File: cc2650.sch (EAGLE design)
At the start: 22 parts, among them IC4 CC2650MODAMOHR, J1 AMP FCI 10103594-0001LF, SW1 SPST_TACT-KMR2, SW2 SPST_TACT-KMR2, U402 TPS62233DRY

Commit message: changed some pins. added bom through eagle.
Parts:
- removed BT1: (no value), SparkFun-Batteries:BATTERY-12MM_SMD
- removed D1: (no value), adafruit:SCHOTTKY-DIODEDO35-7
- removed J1: AMP FCI 10103594-0001LF, SparkFun-Connectors:USB_MICRO-B_HALF_PTH
- removed U$1: (no value), adafruit:CR1220THM
- added BAT: (no value), adafruit:CR1220THM
- added J401: (no value), usb_con-update:USB_MICRO_FLIPPED
- added R4: 100k, adafruit:R-US_R0603
- C1: MPN (none) -> C1005X7R1H104K050BB; OC_NEWARK (none) -> 04X3230
- C2: MPN (none) -> GRT31CC81E475KE01L; OC_NEWARK (none) -> 01AC8998
- C3, C4: MPN (none) -> C0805C105K5RACTU; OC_NEWARK (none) -> 05AC8016
- C5: MPN (none) -> CGA2B2C0G1H102J050BA; OC_NEWARK (none) -> 04X3142
- D2: MPN (none) -> CLMVB-FKA-CFHEHLCBB7A363; OC_NEWARK (none) -> 11X6434
- IC4: MPN (none) -> CC2650MODAMOHR; OC_NEWARK (none) -> 02AC9626
- JP2, JP3, SW1, SW2: OC_NEWARK (none) -> unknown
- JTAG_CONNECTOR: MPN (none) -> FTSH-105-01-F-DV-K; OC_NEWARK (none) -> 45P5160
- L401: MPN (none) -> NR3010T2R2M; OC_NEWARK (none) -> 87K4752
- LED3: MPN (none) -> HSME-C191; OC_NEWARK (none) -> 05M0345
- R1: MF (none) -> VISHAY/DALE; MPN (none) -> CRCW040247K0JNED; OC_NEWARK (none) -> 52K7099
- R2: MPN (none) -> ERA-2AEB471X; OC_NEWARK (none) -> 08N2086
- R3: MPN (none) -> ERJ-U02F33R0X; OC_NEWARK (none) -> 51W3197
- U402: MPN (none) -> TPS62233DRYT; OC_NEWARK (none) -> 37X8886
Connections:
- removed net EZFET_VBUS: C1.1, C2.1, C3.1, D1.C, J1.VBUS, U402.EN, U402.VIN
- removed net N$10: J1.SHIELD, R3.1
- removed net N$3: BT1.+, D1.A
- new net EN: JP3.2, R4.2, U402.EN
- new net VABT: JP3.1
- new net VBAT: BAT.+, BAT.+1
- new net VBUS: C1.1, C2.1, C3.1, J401.VBUS, JP3.3, R4.1, U402.VIN
- net DIO4: now also JP3.8
- net DIO7: now also JP2.11; no longer JP2.12
- net DIO8: now also JP2.10; no longer JP2.11
- net DIO9_CS: now also JP2.7; no longer JP2.10
- net EZFET_VCC: now also JP3.4; no longer JP3.1
- net GND: now also BAT.-, J401.GND, R3.1; no longer BT1.-, J1.GND
- net PWR_LED_JMPR: now also JP3.7; no longer JP3.4
- net VCC: now also JP3.5, JP3.6; no longer JP3.2, JP3.3
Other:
- note added: "Remove jumper from 4&5 to measure current. Remove jumper from 6 & 7 to disable PWR LED."
- note removed: "Use jumper on pins 1 & 2 for operation. Remove jumper to measure current."
- moved on the sheet: C3, C4, L401, U402

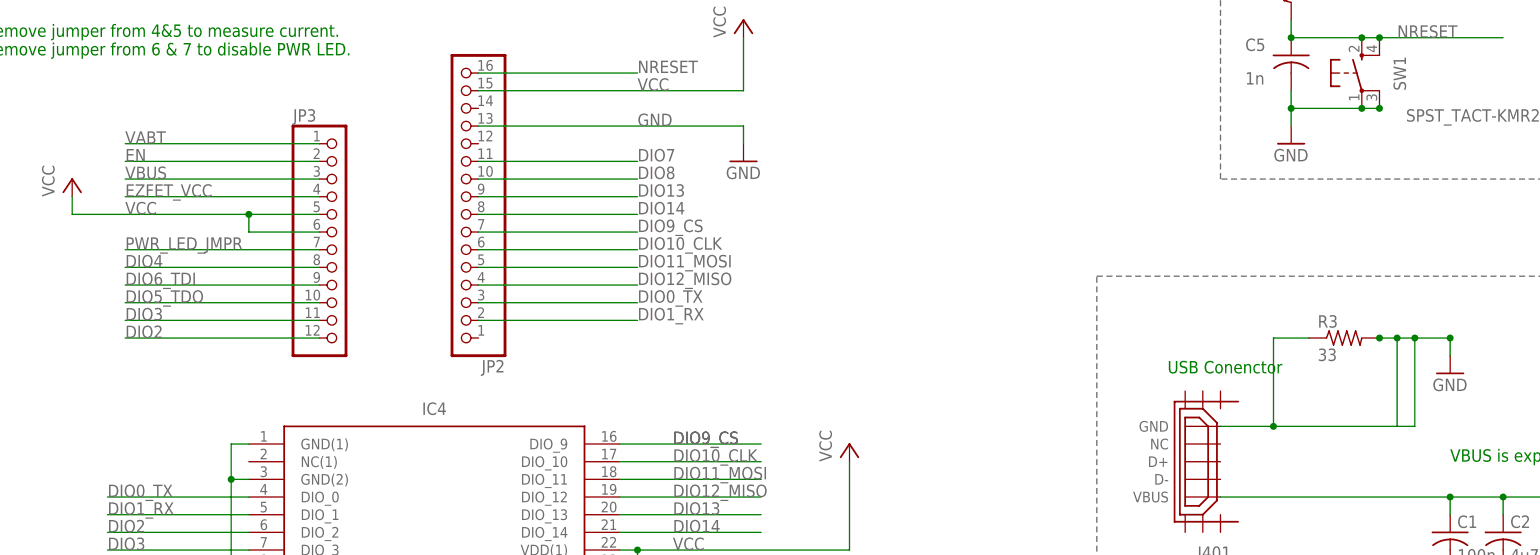
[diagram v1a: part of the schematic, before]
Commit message: added bom though eagle. added gnd planes. replaced some symbols.
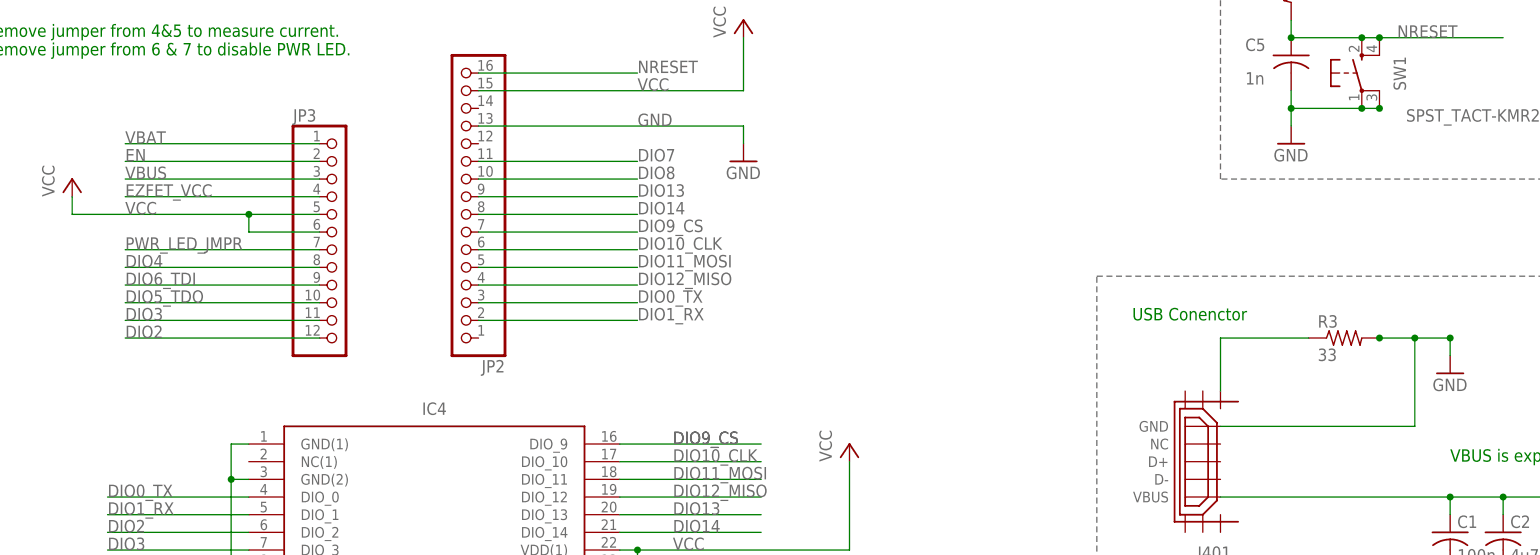
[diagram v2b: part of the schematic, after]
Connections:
- removed net VABT: JP3.1
- new net N$1: J401.SHIELD1, R3.1
- net GND: no longer R3.1
- net VBAT: now also JP3.1
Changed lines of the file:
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@@
 <sheet>
 <plain>
-<text x="27.94" y="17.78" size="1.778" layer="91">USB Conenctor</text>
+<text x="22.86" y="25.4" size="1.778" layer="91">USB Conenctor</text>
 <text x="36.322" y="86.106" size="2.54" layer="95">RESET</text>
 <wire x1="35.56" y1="45.72" x2="35.56" y2="90.17" width="0.1524" layer="95" style="shortdash"/>
@@
 <wire x1="68.58" y1="20.32" x2="68.58" y2="22.86" width="0.1524" layer="91"/>
 <wire x1="68.58" y1="22.86" x2="63.5" y2="22.86" width="0.1524" layer="91"/>
-<wire x1="63.5" y1="22.86" x2="60.96" y2="22.86" width="0.1524" layer="91"/>
-<wire x1="60.96" y1="22.86" x2="60.96" y2="10.16" width="0.1524" layer="91"/>
-<wire x1="58.42" y1="22.86" x2="60.96" y2="22.86" width="0.1524" layer="91"/>
-<junction x="60.96" y="22.86"/>
+<wire x1="58.42" y1="22.86" x2="63.5" y2="22.86" width="0.1524" layer="91"/>
 <wire x1="63.5" y1="22.86" x2="63.5" y2="10.16" width="0.1524" layer="91"/>
 <junction x="63.5" y="22.86"/>
-<wire x1="63.5" y1="10.16" x2="43.18" y2="10.16" width="0.1524" layer="91"/>
+<wire x1="63.5" y1="10.16" x2="35.56" y2="10.16" width="0.1524" layer="91"/>
 <pinref part="R3" gate="G$1" pin="2"/>
 <junction x="58.42" y="22.86"/>
 <junction x="68.58" y="22.86"/>
 <pinref part="J401" gate="G$1" pin="GND"/>
-<pinref part="R3" gate="G$1" pin="1"/>
-<wire x1="43.18" y1="10.16" x2="35.56" y2="10.16" width="0.1524" layer="91"/>
-<wire x1="48.26" y1="22.86" x2="43.18" y2="22.86" width="0.1524" layer="91"/>
-<wire x1="43.18" y1="22.86" x2="43.18" y2="10.16" width="0.1524" layer="91"/>
-<junction x="43.18" y="10.16"/>
 </segment>
 <segment>
@@
 <label x="228.6" y="10.16" size="1.778" layer="95"/>
 </segment>
-</net>
-<net name="VABT" class="0">
 <segment>
 <pinref part="JP3" gate="G$1" pin="1"/>
@@
 </segment>
 </net>
+<net name="N$1" class="0">
+<segment>
+<pinref part="R3" gate="G$1" pin="1"/>
+<pinref part="J401" gate="G$1" pin="SHIELD1"/>
+<wire x1="35.56" y1="15.24" x2="35.56" y2="22.86" width="0.1524" layer="91"/>
+<wire x1="35.56" y1="22.86" x2="48.26" y2="22.86" width="0.1524" layer="91"/>
+</segment>
+</net>

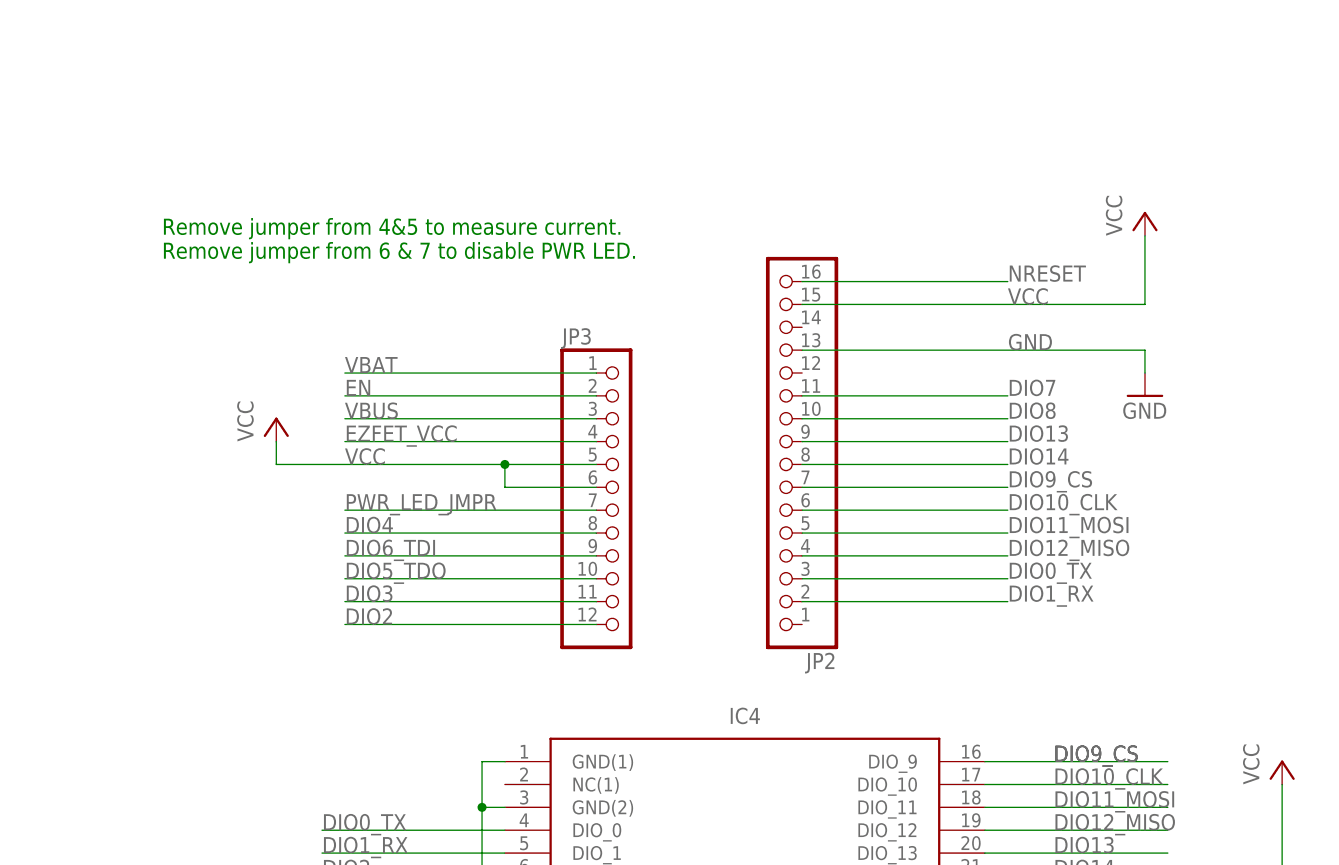
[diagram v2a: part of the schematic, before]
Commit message: added bom though eagle. added gnd planes. rearranged board.
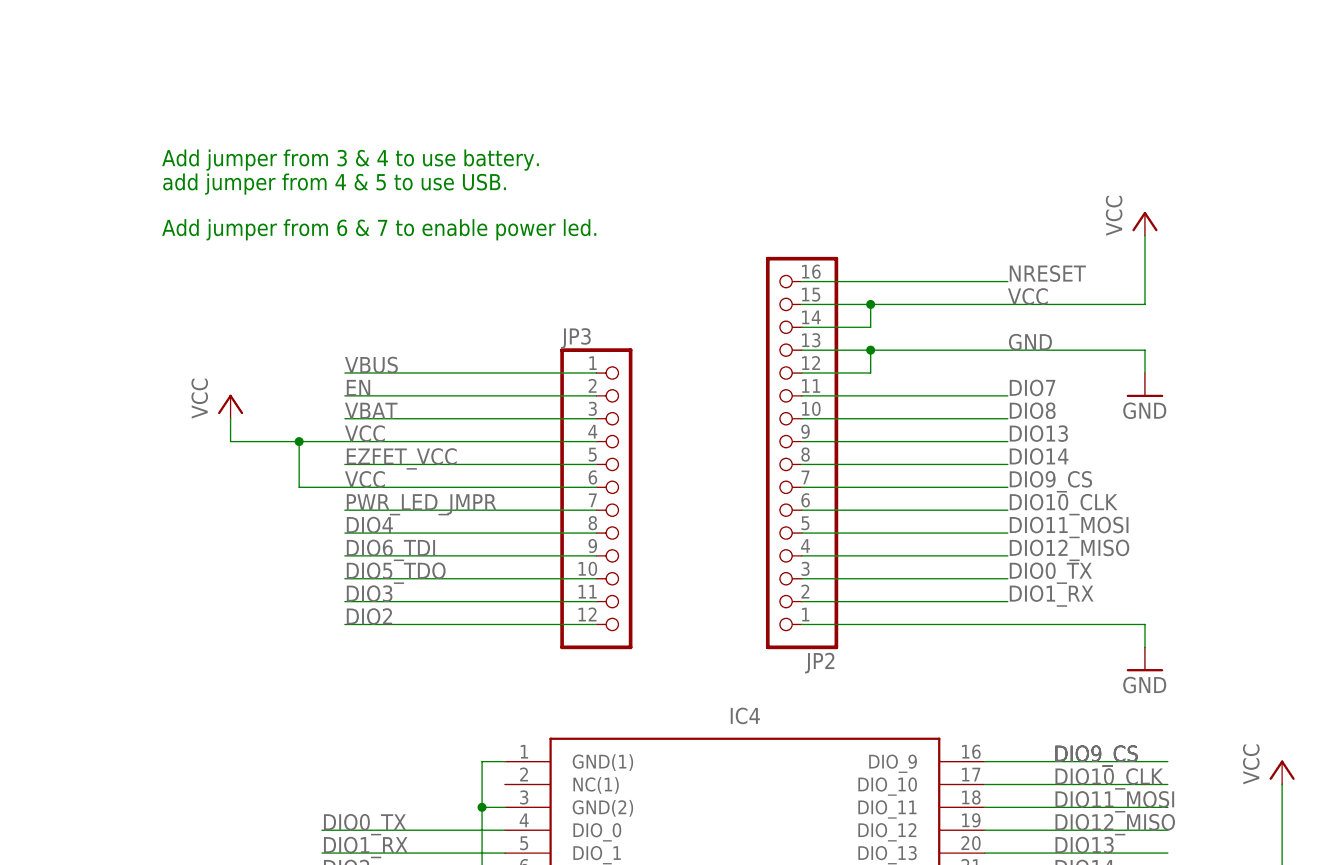
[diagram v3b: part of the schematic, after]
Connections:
- net EZFET_VCC: now also JP3.5; no longer JP3.4
- net GND: now also JP2.1, JP2.12
- net VBAT: now also JP3.3; no longer JP3.1
- net VBUS: now also JP3.1; no longer JP3.3
- net VCC: now also JP2.14, JP3.4; no longer JP3.5
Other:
- note added: "Add jumper from 3 & 4 to use battery. add jumper from 4 & 5 to use USB."
- note added: "Add jumper from 6 & 7 to enable power led."
- note removed: "Remove jumper from 4&5 to measure current. Remove jumper from 6 & 7 to disable PWR LED."
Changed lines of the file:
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@@
 <attribute name="OC_NEWARK" value="84Y6712"/>
 </part>
+<part name="GND6" library="supply1" library_urn="urn:adsk.eagle:library:371" deviceset="GND" device=""/>
 </parts>
 <sheets>
@@
 <wire x1="17.78" y1="-92.71" x2="127" y2="-92.71" width="0.1524" layer="95" style="shortdash"/>
 <text x="60.96" y="-45.72" size="1.778" layer="91">GPIO Programmable</text>
-<text x="-142.24" y="63.5" size="1.778" layer="91">Remove jumper from 4&amp;5 to measure current.
-Remove jumper from 6 &amp; 7 to disable PWR LED.</text>
+<text x="-142.24" y="71.12" size="1.778" layer="91">Add jumper from 3 &amp; 4 to use battery.
+add jumper from 4 &amp; 5 to use USB.</text>
+<text x="-142.24" y="66.04" size="1.778" layer="91">Add jumper from 6 &amp; 7 to enable power led.</text>
 </plain>
 <instances>
@@
 <attribute name="MPN" x="154.94" y="-7.62" size="1.778" layer="96" display="off"/>
 </instance>
-<instance part="P+2" gate="VCC" x="-129.54" y="45.72"/>
+<instance part="P+2" gate="VCC" x="-134.62" y="48.26"/>
 <instance part="J401" gate="G$1" x="33.02" y="5.08" rot="R180">
 <attribute name="OC_NEWARK" x="33.02" y="5.08" size="1.778" layer="96" display="off"/>
@@
 <attribute name="MPN" x="33.02" y="5.08" size="1.778" layer="96" display="off"/>
 </instance>
+<instance part="GND6" gate="1" x="-33.02" y="17.78"/>
 </instances>
 <busses>
@@
 <wire x1="-33.02" y1="53.34" x2="-33.02" y2="50.8" width="0.1524" layer="91"/>
 <pinref part="JP2" gate="A" pin="13"/>
-<wire x1="-71.12" y1="53.34" x2="-33.02" y2="53.34" width="0.1524" layer="91"/>
+<wire x1="-71.12" y1="53.34" x2="-63.5" y2="53.34" width="0.1524" layer="91"/>
 <label x="-48.26" y="53.34" size="1.778" layer="95"/>
+<pinref part="JP2" gate="A" pin="12"/>
+<wire x1="-63.5" y1="53.34" x2="-33.02" y2="53.34" width="0.1524" layer="91"/>
+<wire x1="-71.12" y1="50.8" x2="-63.5" y2="50.8" width="0.1524" layer="91"/>
+<wire x1="-63.5" y1="50.8" x2="-63.5" y2="53.34" width="0.1524" layer="91"/>
+<junction x="-63.5" y="53.34"/>
 </segment>
 <segment>
@@
 <pinref part="BAT" gate="G$1" pin="-"/>
 <wire x1="228.6" y1="-22.86" x2="228.6" y2="-15.24" width="0.1524" layer="91"/>
+</segment>
+<segment>
+<pinref part="GND6" gate="1" pin="GND"/>
+<wire x1="-33.02" y1="20.32" x2="-33.02" y2="22.86" width="0.1524" layer="91"/>
+<pinref part="JP2" gate="A" pin="1"/>
+<wire x1="-71.12" y1="22.86" x2="-33.02" y2="22.86" width="0.1524" layer="91"/>
 </segment>
 </net>
@@
 </segment>
 <segment>
-<pinref part="JP3" gate="G$1" pin="4"/>
-<wire x1="-93.98" y1="43.18" x2="-121.92" y2="43.18" width="0.1524" layer="91"/>
-<label x="-121.92" y="43.18" size="1.778" layer="95"/>
+<pinref part="JP3" gate="G$1" pin="5"/>
+<wire x1="-93.98" y1="40.64" x2="-121.92" y2="40.64" width="0.1524" layer="91"/>
+<label x="-121.92" y="40.64" size="1.778" layer="95"/>
 </segment>
 </net>
@@
 <segment>
 <pinref part="JP2" gate="A" pin="15"/>
-<wire x1="-71.12" y1="58.42" x2="-33.02" y2="58.42" width="0.1524" layer="91"/>
+<wire x1="-71.12" y1="58.42" x2="-63.5" y2="58.42" width="0.1524" layer="91"/>
 <label x="-48.26" y="58.42" size="1.778" layer="95"/>
+<wire x1="-63.5" y1="58.42" x2="-33.02" y2="58.42" width="0.1524" layer="91"/>
 <wire x1="-33.02" y1="58.42" x2="-33.02" y2="66.04" width="0.1524" layer="91"/>
 <pinref part="P+1" gate="VCC" pin="VCC"/>
+<pinref part="JP2" gate="A" pin="14"/>
+<wire x1="-71.12" y1="55.88" x2="-63.5" y2="55.88" width="0.1524" layer="91"/>
+<wire x1="-63.5" y1="55.88" x2="-63.5" y2="58.42" width="0.1524" layer="91"/>
+<junction x="-63.5" y="58.42"/>
 </segment>
 <segment>
@@
 </segment>
 <segment>
-<pinref part="JP3" gate="G$1" pin="5"/>
-<wire x1="-93.98" y1="40.64" x2="-104.14" y2="40.64" width="0.1524" layer="91"/>
-<label x="-121.92" y="40.64" size="1.778" layer="95"/>
-<wire x1="-104.14" y1="40.64" x2="-129.54" y2="40.64" width="0.1524" layer="91"/>
-<wire x1="-129.54" y1="40.64" x2="-129.54" y2="43.18" width="0.1524" layer="91"/>
+<wire x1="-134.62" y1="43.18" x2="-134.62" y2="45.72" width="0.1524" layer="91"/>
 <pinref part="P+2" gate="VCC" pin="VCC"/>
+<pinref part="JP3" gate="G$1" pin="4"/>
+<wire x1="-93.98" y1="43.18" x2="-127" y2="43.18" width="0.1524" layer="91"/>
+<label x="-121.92" y="43.18" size="1.778" layer="95"/>
 <pinref part="JP3" gate="G$1" pin="6"/>
-<wire x1="-93.98" y1="38.1" x2="-104.14" y2="38.1" width="0.1524" layer="91"/>
-<wire x1="-104.14" y1="38.1" x2="-104.14" y2="40.64" width="0.1524" layer="91"/>
-<junction x="-104.14" y="40.64"/>
+<wire x1="-127" y1="43.18" x2="-134.62" y2="43.18" width="0.1524" layer="91"/>
+<wire x1="-93.98" y1="38.1" x2="-127" y2="38.1" width="0.1524" layer="91"/>
+<label x="-121.92" y="38.1" size="1.778" layer="95"/>
+<wire x1="-127" y1="38.1" x2="-127" y2="43.18" width="0.1524" layer="91"/>
+<junction x="-127" y="43.18"/>
 </segment>
 </net>
@@
 </segment>
 <segment>
-<pinref part="JP3" gate="G$1" pin="1"/>
-<wire x1="-93.98" y1="50.8" x2="-121.92" y2="50.8" width="0.1524" layer="91"/>
-<label x="-121.92" y="50.8" size="1.778" layer="95"/>
+<pinref part="JP3" gate="G$1" pin="3"/>
+<wire x1="-93.98" y1="45.72" x2="-121.92" y2="45.72" width="0.1524" layer="91"/>
+<label x="-121.92" y="45.72" size="1.778" layer="95"/>
 </segment>
 </net>
@@
 </segment>
 <segment>
-<pinref part="JP3" gate="G$1" pin="3"/>
-<wire x1="-93.98" y1="45.72" x2="-121.92" y2="45.72" width="0.1524" layer="91"/>
-<label x="-121.92" y="45.72" size="1.778" layer="95"/>
-</segment>
-</net>
+<pinref part="JP3" gate="G$1" pin="1"/>
+<wire x1="-93.98" y1="50.8" x2="-121.92" y2="50.8" width="0.1524" layer="91"/>
+<label x="-121.92" y="50.8" size="1.778" layer="95"/>
+</segment>
+</net>
